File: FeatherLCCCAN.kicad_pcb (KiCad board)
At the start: 2 copper layers, 50.8 x 22.9 mm, 1 part

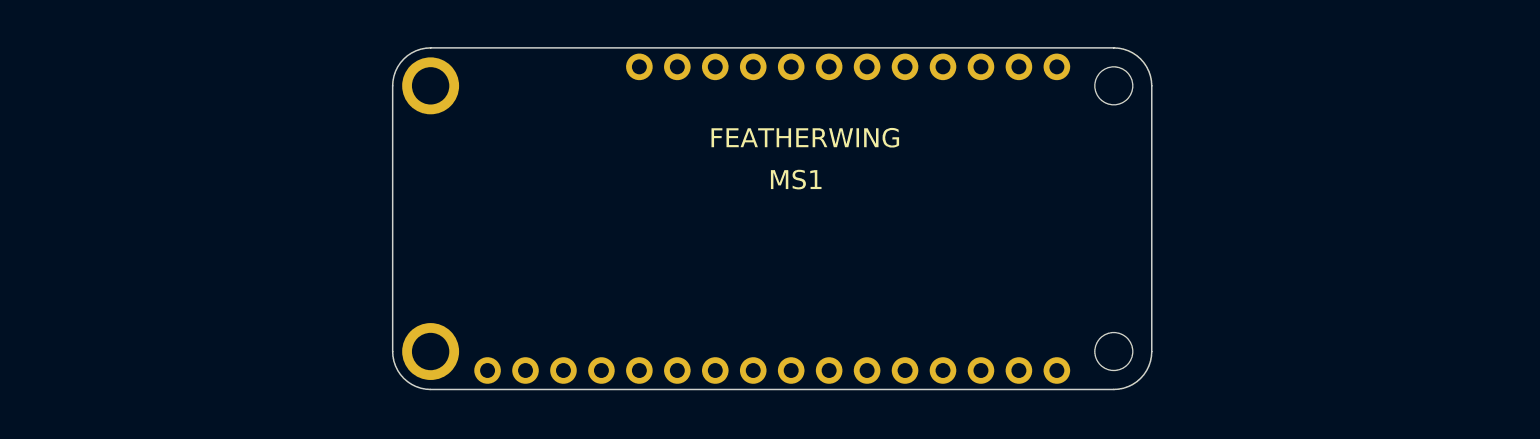
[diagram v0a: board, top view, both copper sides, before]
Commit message: Completed LCC CAN Feather Wing.
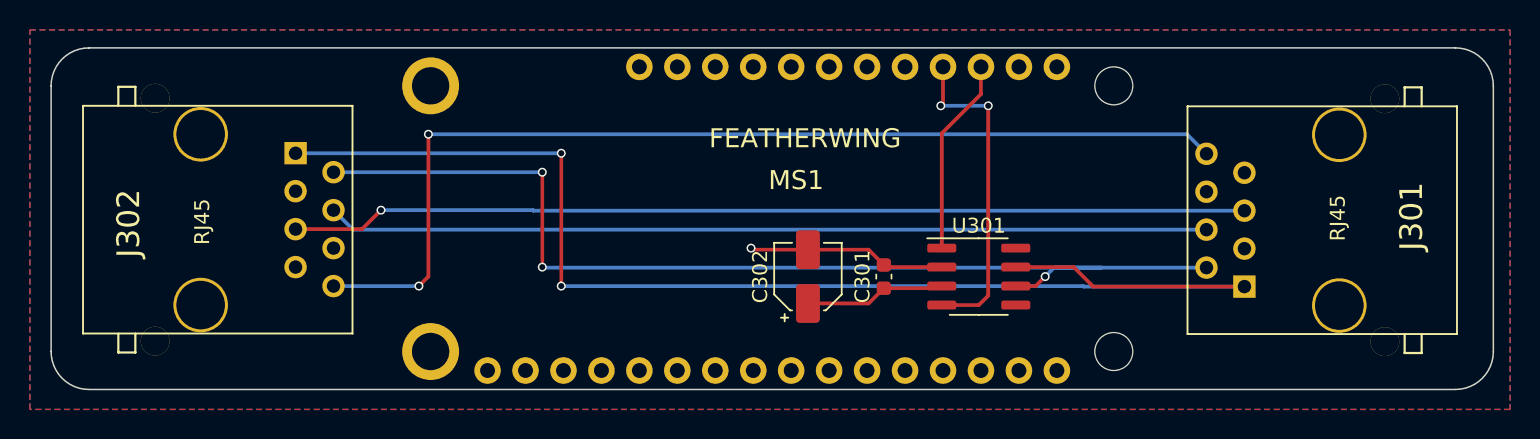
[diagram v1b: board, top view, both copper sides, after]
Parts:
- added C301: .1 uf, Capacitor_SMD:C_0603_1608Metric, F.Cu at (156.2, 83.8)
- added C302: 15 uf 15V, Capacitor_SMD:CP_Elec_4x5.7, F.Cu at (151.1, 83.8)
- added J301: RJ45, RJ45:RJ45_8N-S, F.Cu at (186.7, 80.0)
- added J302: RJ45, RJ45:RJ45_8N-S, F.Cu at (110.5, 80.0)
- added U301: TCAN332DR, Package_SO:SOIC-8_3.9x4.9mm_P1.27mm, F.Cu at (162.6, 83.8)
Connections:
- MS1 pad 19: /N$23 -> /CAN_TX
- MS1 pad 2: /3V -> +3V3
- MS1 pad 20: /N$22 -> /CAN_RX
- MS1 pad 4: /GND -> GND
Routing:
- net /CANH: track 0.00 -> 88.2 mm, vias 0 -> 2
- net /CANL: track 0.00 -> 71.0 mm, vias 0 -> 3
- net Net-(J301-Pad8): track 0.00 -> 68.7 mm, vias 0 -> 2
- net Net-(J301-Pad5): track 0.00 -> 64.0 mm, vias 0 -> 1
- net Net-(J301-Pad4): track 0.00 -> 59.0 mm
- net /CAN_RX: track 0.00 -> 21.9 mm, vias 0 -> 2
- net GND: track 0.00 -> 13.3 mm, vias 0 -> 1
- net /CAN_TX: track 0.00 -> 13.2 mm
- net +3V3: track 0.00 -> 9.44 mm
- added copper zone on F.Cu, net +3V3
- added copper zone on B.Cu, net GND
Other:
- board size 50.8 x 22.9 mm -> 96.5 x 22.9 mm

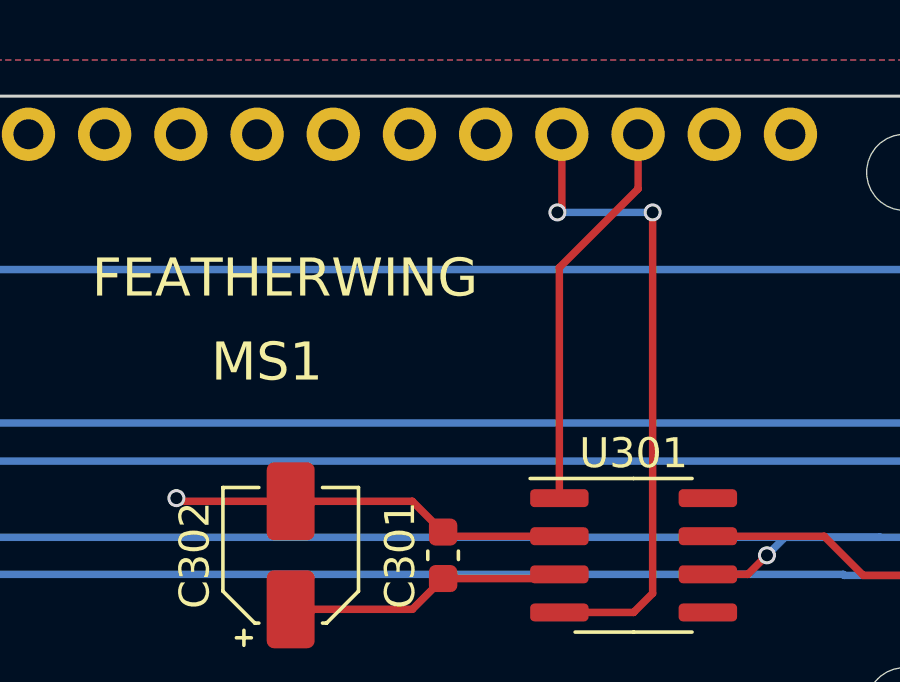
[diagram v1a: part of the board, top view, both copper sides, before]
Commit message: Change CAN pins (allow for Adafruit 3.5" FeatherWing TFT & TouchScreen).
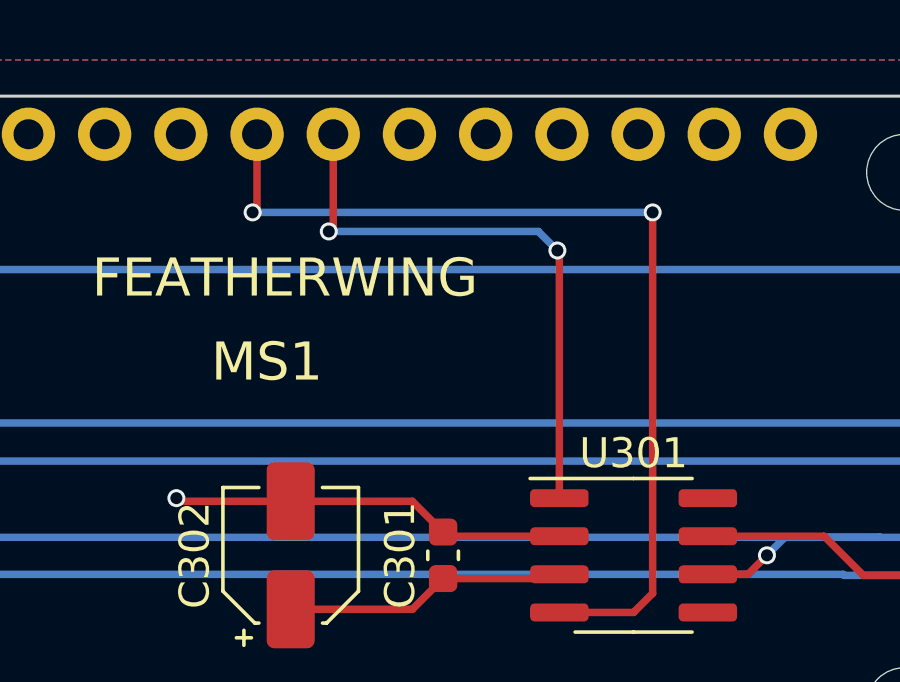
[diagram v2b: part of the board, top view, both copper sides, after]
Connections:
- MS1 pad 19: /CAN_TX -> /N$23
- MS1 pad 20: /CAN_RX -> /N$22
- MS1 pad 23: /N$19 -> /CAN_TX
- MS1 pad 24: /N$5 -> /CAN_RX
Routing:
- net /CAN_RX: track 21.9 -> 32.1 mm
- net /CAN_TX: track 13.2 -> 19.5 mm, vias 0 -> 2
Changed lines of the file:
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@@
   (net 5 "/N$21")
   (net 6 "/N$20")
-  (net 7 "/N$19")
-  (net 8 "/N$5")
+  (net 7 "/N$23")
+  (net 8 "/N$22")
   (net 9 "/N$3")
   (net 10 "/USB")
@@
       (net 2 "/N$24") (pinfunction "GPIOSCL") (pintype "bidirectional"))
     (pad "19" thru_hole circle (at 39.37 -21.59) (size 1.778 1.778) (drill 0.99822) (layers *.Cu *.Paste *.Mask)
-      (net 31 "/CAN_TX") (pinfunction "GPIO5") (pintype "bidirectional"))
+      (net 7 "/N$23") (pinfunction "GPIO5") (pintype "bidirectional"))
     (pad "20" thru_hole circle (at 36.83 -21.59) (size 1.778 1.778) (drill 0.99822) (layers *.Cu *.Paste *.Mask)
-      (net 32 "/CAN_RX") (pinfunction "GPIO6") (pintype "bidirectional"))
+      (net 8 "/N$22") (pinfunction "GPIO6") (pintype "bidirectional"))
     (pad "21" thru_hole circle (at 34.29 -21.59) (size 1.778 1.778) (drill 0.99822) (layers *.Cu *.Paste *.Mask)
       (net 5 "/N$21") (pinfunction "GPIO9") (pintype "bidirectional"))
@@
       (net 6 "/N$20") (pinfunction "GPIO10") (pintype "bidirectional"))
     (pad "23" thru_hole circle (at 29.21 -21.59) (size 1.778 1.778) (drill 0.99822) (layers *.Cu *.Paste *.Mask)
-      (net 7 "/N$19") (pinfunction "GPIO11") (pintype "bidirectional"))
+      (net 31 "/CAN_TX") (pinfunction "GPIO11") (pintype "bidirectional"))
     (pad "24" thru_hole circle (at 26.67 -21.59) (size 1.778 1.778) (drill 0.99822) (layers *.Cu *.Paste *.Mask)
-      (net 8 "/N$5") (pinfunction "GPIO12") (pintype "bidirectional"))
+      (net 32 "/CAN_RX") (pinfunction "GPIO12") (pintype "bidirectional"))
     (pad "25" thru_hole circle (at 24.13 -21.59) (size 1.778 1.778) (drill 0.99822) (layers *.Cu *.Paste *.Mask)
       (net 9 "/N$3") (pinfunction "GPIO13") (pintype "bidirectional"))
@@
   (segment (start 116.84 75.565) (end 134.62 75.565) (width 0.25) (layer "B.Cu") (net 30))
   (segment (start 134.62 84.455) (end 169.545 84.455) (width 0.25) (layer "B.Cu") (net 30))
-  (segment (start 162.7084 71.6066) (end 160.085 74.23) (width 0.25) (layer "F.Cu") (net 31))
-  (segment (start 162.7084 69.7848) (end 162.7084 71.6066) (width 0.25) (layer "F.Cu") (net 31))
-  (segment (start 160.085 74.23) (end 160.085 81.915) (width 0.25) (layer "F.Cu") (net 31))
+  (segment (start 160.085 73.725) (end 160.085 81.915) (width 0.25) (layer "F.Cu") (net 31))
+  (segment (start 160.02 73.66) (end 160.085 73.725) (width 0.25) (layer "F.Cu") (net 31))
+  (segment (start 152.5484 72.8766) (end 152.5484 69.7848) (width 0.25) (layer "F.Cu") (net 31))
+  (segment (start 152.4 73.025) (end 152.5484 72.8766) (width 0.25) (layer "F.Cu") (net 31))
+  (via (at 160.02 73.66) (size 0.6) (drill 0.4) (layers "F.Cu" "B.Cu") (net 31))
+  (via (at 152.4 73.025) (size 0.6) (drill 0.4) (layers "F.Cu" "B.Cu") (net 31))
+  (segment (start 159.385 73.025) (end 152.4 73.025) (width 0.25) (layer "B.Cu") (net 31))
+  (segment (start 160.02 73.66) (end 159.385 73.025) (width 0.25) (layer "B.Cu") (net 31))
+  (segment (start 150.0084 72.2416) (end 150.0084 69.7848) (width 0.25) (layer "F.Cu") (net 32))
   (segment (start 163.195 72.39) (end 163.195 85.09) (width 0.25) (layer "F.Cu") (net 32))
-  (segment (start 160.1684 72.2416) (end 160.02 72.39) (width 0.25) (layer "F.Cu") (net 32))
   (segment (start 162.56 85.725) (end 160.085 85.725) (width 0.25) (layer "F.Cu") (net 32))
   (segment (start 163.195 85.09) (end 162.56 85.725) (width 0.25) (layer "F.Cu") (net 32))
-  (segment (start 160.1684 69.7848) (end 160.1684 72.2416) (width 0.25) (layer "F.Cu") (net 32))
+  (segment (start 149.86 72.39) (end 150.0084 72.2416) (width 0.25) (layer "F.Cu") (net 32))
   (via (at 163.195 72.39) (size 0.6) (drill 0.4) (layers "F.Cu" "B.Cu") (net 32))
-  (via (at 160.02 72.39) (size 0.6) (drill 0.4) (layers "F.Cu" "B.Cu") (net 32))
-  (segment (start 160.02 72.39) (end 163.195 72.39) (width 0.25) (layer "B.Cu") (net 32))
+  (via (at 149.86 72.39) (size 0.6) (drill 0.4) (layers "F.Cu" "B.Cu") (net 32))
+  (segment (start 149.86 72.39) (end 163.195 72.39) (width 0.25) (layer "B.Cu") (net 32))
   (segment (start 125.73 74.295) (end 125.73 83.82) (width 0.25) (layer "F.Cu") (net 35))
   (segment (start 125.73 83.82) (end 125.095 84.455) (width 0.25) (layer "F.Cu") (net 35))
